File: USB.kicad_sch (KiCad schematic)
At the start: 55 parts, among them J1 USB_C_Receptacle_USB2.0, J2 USB_A, J3 USB_A, J4 USB_A, U5 NUP2202, U6 NUP2202, U7 NUP2202, U8 NUP2202, Y1 12MHz

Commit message: Add files via upload
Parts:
- removed U3: ~, Package_QFP:LQFP-48_7x7mm_P0.5mm, symbol GL850G-HH:GL850G-HH
- added U9: ~, Package_SO:SSOP-28_5.3x10.2mm_P0.65mm, symbol GL850G-HH:GL850G-HH
- C22, C24, C26: footprint Capacitor_SMD:CP_Elec_6.3x7.7 -> Capacitor_SMD:C_1206_3216Metric_Pad1.33x1.80mm_HandSolder
- R5, R7: footprint Resistor_SMD:R_0805_2012Metric_Pad1.20x1.40mm_HandSolder -> Resistor_SMD:R_0603_1608Metric_Pad0.98x0.95mm_HandSolder
- TH1, TH2, TH4: footprint Fuse:Fuse_0805_2012Metric_Pad1.15x1.40mm_HandSolder -> Fuse:Fuse_0402_1005Metric_Pad0.77x0.64mm_HandSolder
- U5, U6, U7, U8: footprint Package_TO_SOT_SMD:TSOT-23-6 -> Package_TO_SOT_SMD:SOT-363_SC-70-6_Handsoldering
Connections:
- net +5V: now also U9.23 (V5)
- net AVDD: now also U9.1 (AVDD), U9.10 (AVDD), U9.5 (AVDD)
- net DVDD: now also U9.16 (DVDD), U9.24 (V33)
- net D_N0: now also U9.25 (DM0)
- net D_N1: now also U9.27 (DM1)
- net D_N2: now also U9.2 (DM2)
- net D_N3: now also U9.8 (DM3)
- net D_P0: now also U9.26 (DP0)
- net D_P1: now also U9.28 (DP1)
- net D_P2: now also U9.3 (DP2)
- net D_P3: now also U9.9 (DP3)
- net OVERCUR1: now also U9.21 (OVCUR1)
- net PGANG: now also U9.18 (PGANG)
- net RESET: now also U9.13 (RESET)
- net USBD_N: now also U9.11 (DM4)
- net USBD_P: now also U9.12 (DP4)
- net X1: now also U9.6 (X1)
- net X2: now also U9.7 (X2)
- net at R5.2: now also U9.4 (RREF)
- net AGND renamed GND
- net GND: now also U9.15 (GND)

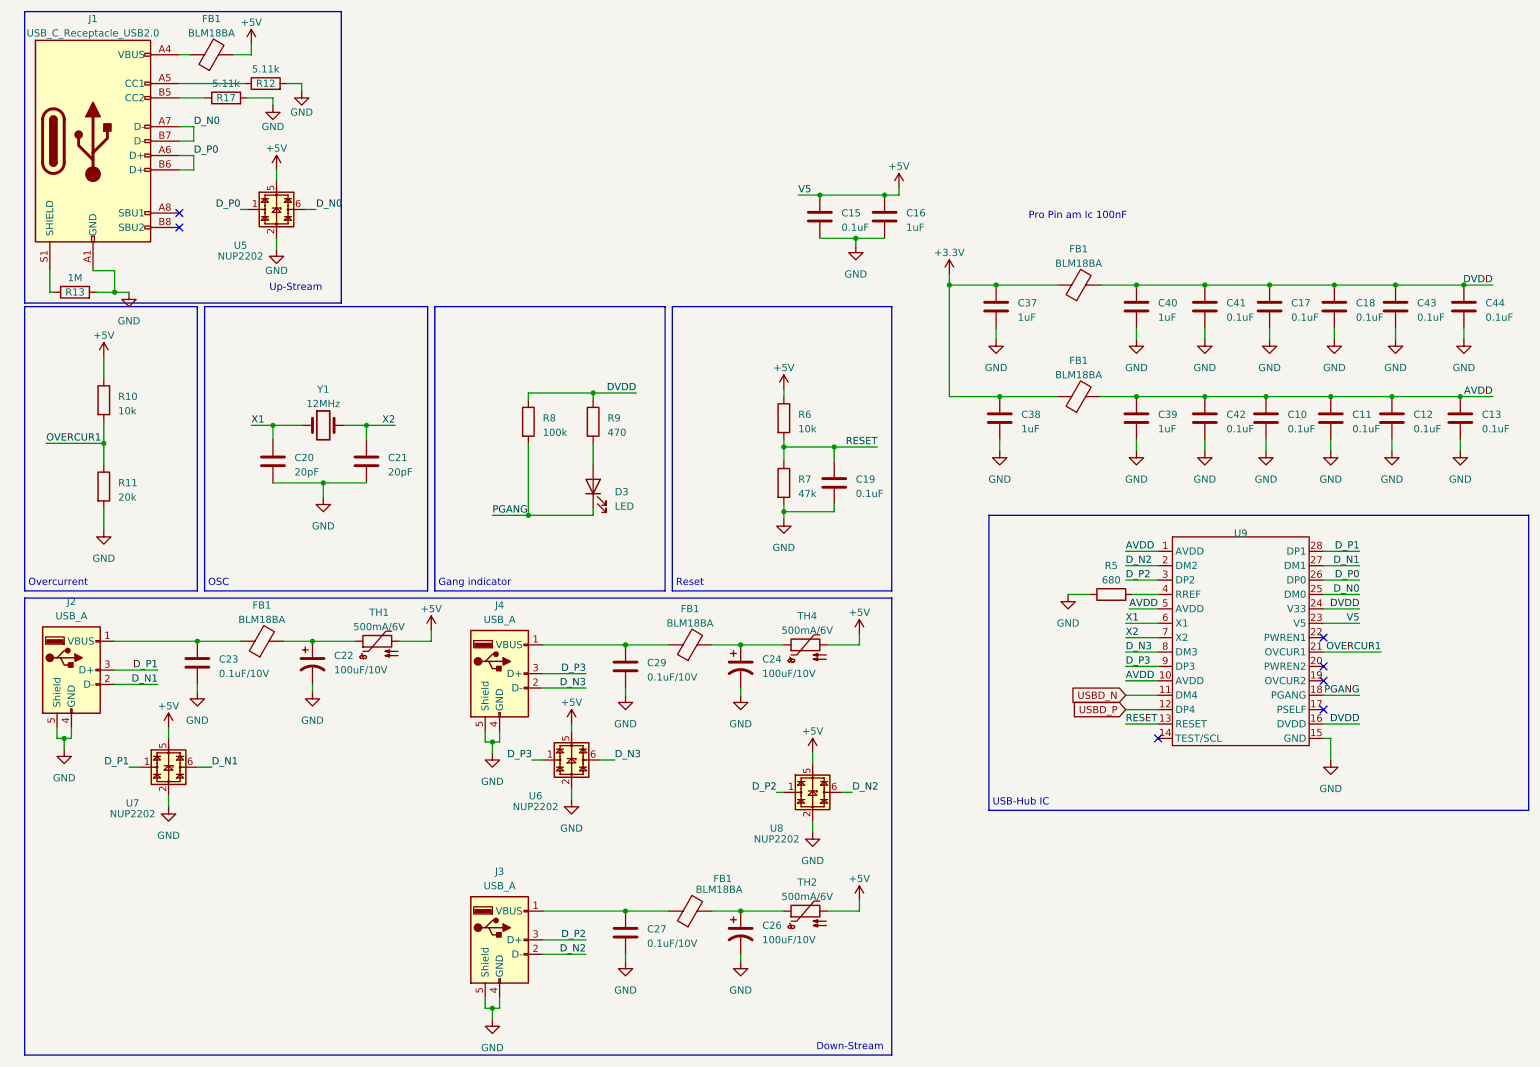
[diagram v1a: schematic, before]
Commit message: Add STM32 Symbol and changed schematic
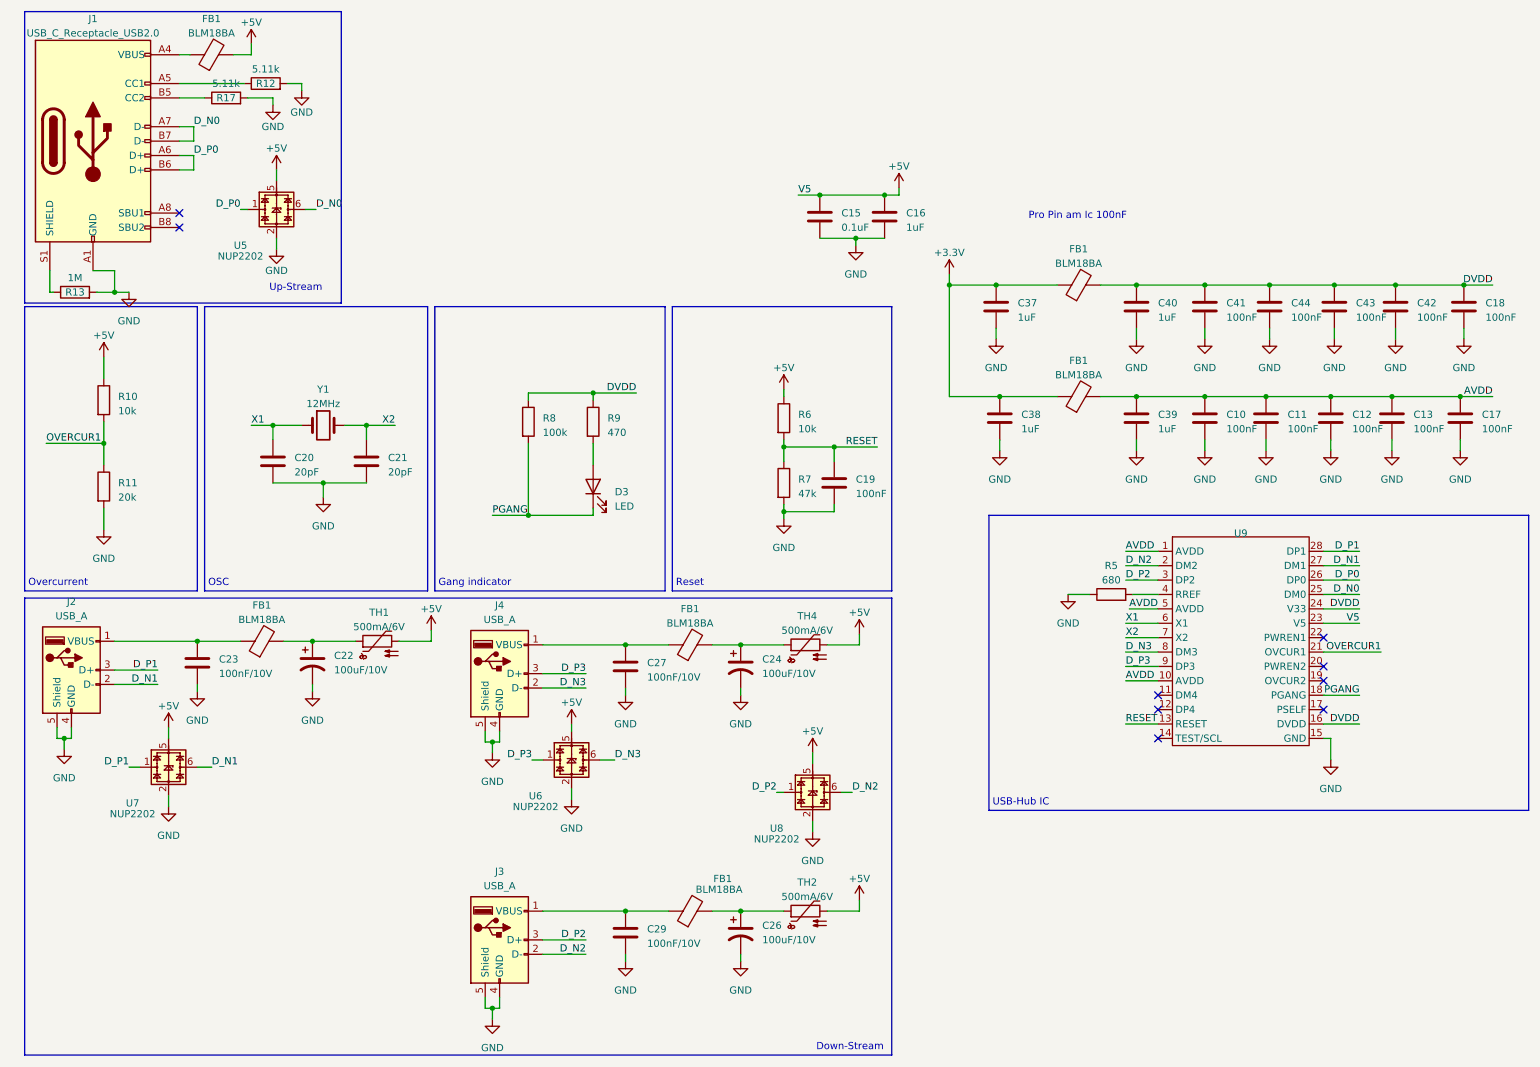
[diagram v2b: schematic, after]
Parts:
- C10, C11, C12, C13, C17, C18, C19, C41, C42, C43, C44: value 0.1uF -> 100nF
- C23, C27, C29: value 0.1uF/10V -> 100nF/10V
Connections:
- net AVDD: now also C17.2; no longer C42.2
- net DVDD: now also C42.2; no longer C17.2
- net GND: now also C19.1; no longer C19.2
- net RESET: now also C19.2; no longer C19.1
- net at FB1.1, J4.1 (VBUS): now also C27.1; no longer C29.1
- net at FB1.1, J3.1 (VBUS): now also C29.1; no longer C27.1
- net USBD_N: no longer names the net of U9.11 (DM4)
- net USBD_P: no longer names the net of U9.12 (DP4)
- no-connect marks 7 -> 9
